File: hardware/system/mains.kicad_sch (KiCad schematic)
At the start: 10 parts, among them M1 Mains inlet, M2 RCD, M3 E-stop mushroom NC, M4 PSU 24-36 V, M5 Bit-change key switch, M6 Router contactor, M7 RC snubber, M8 Router socket, M9 PE: enclosure + lift frame

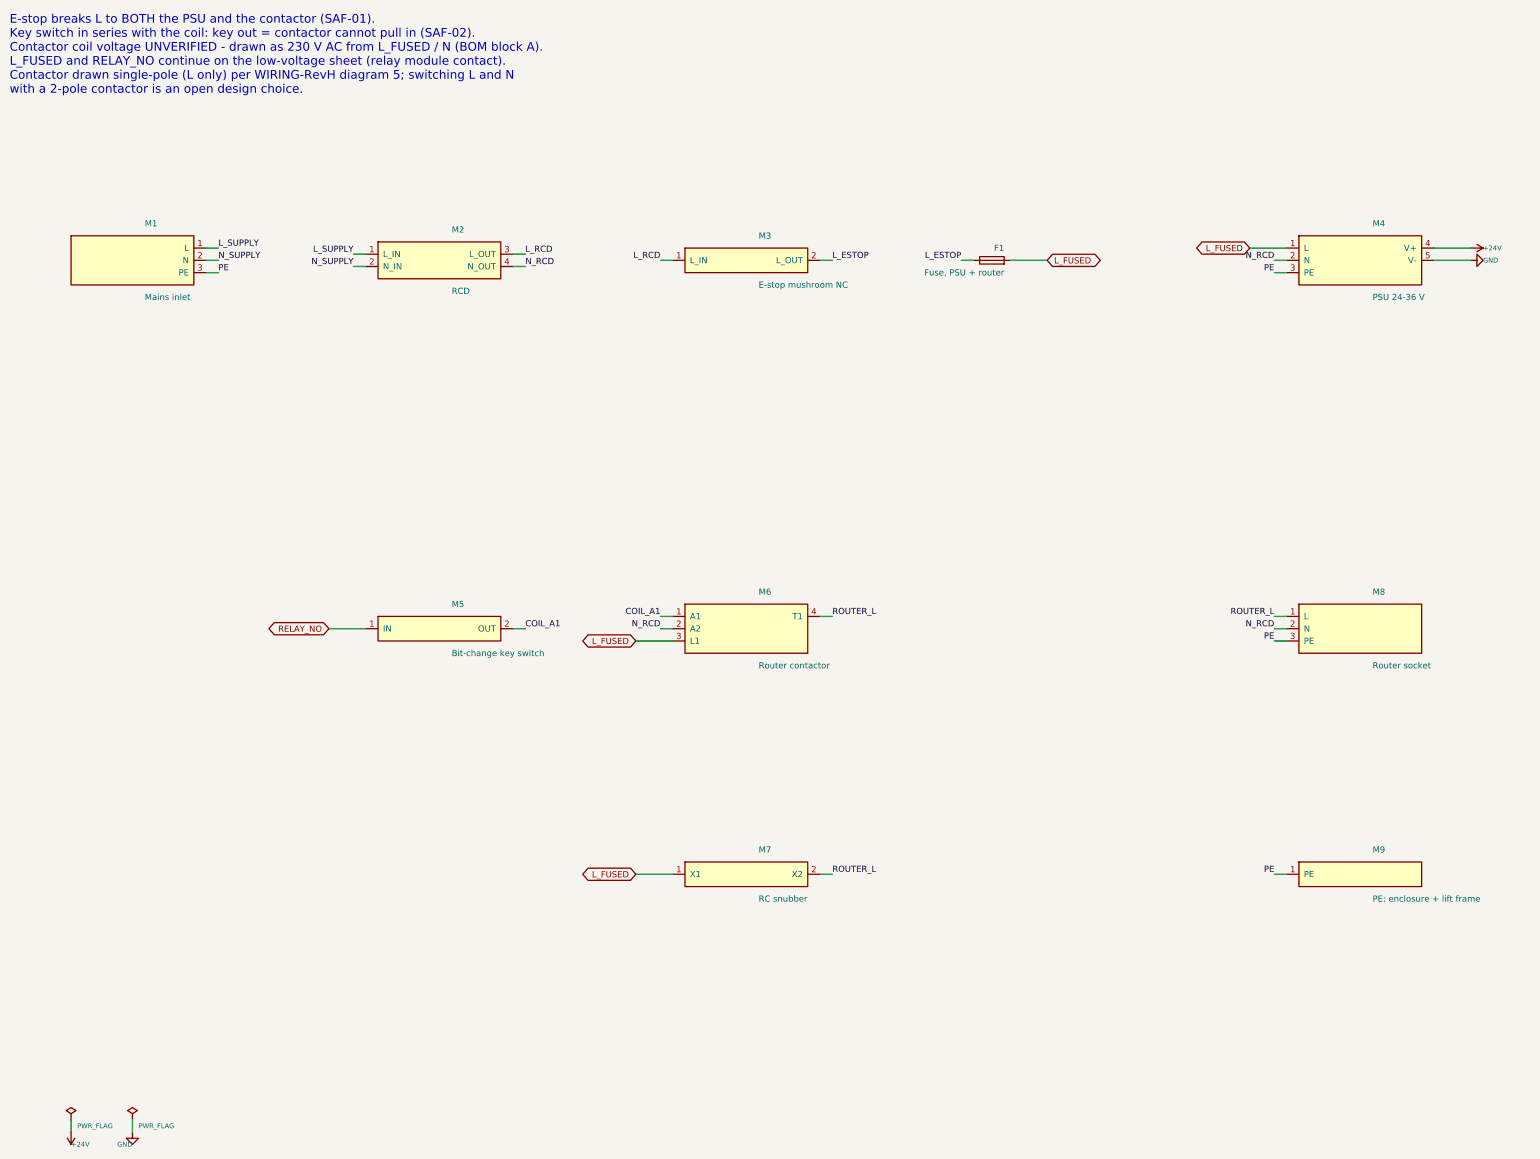
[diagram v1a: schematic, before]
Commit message: fix(hardware): put the fuse before the E-stop and switch L and N at the contactor
Decided 2026-09-14: the mains order is RCD, fuse, E-stop, and the
router contactor is 2-pole so the router is isolated whichever way
round the supply is wired. The live net after the E-stop is renamed
L_ESTOP. BOM block A, WIRING-RevH diagrams 1 and 5 and the spec now
agree with the drawing; the key switch stays between the relay
contact and coil A1.

Co-Authored-By: Claude Opus 5 (1M context) <noreply@anthropic.com>
Claude-Session: https://claude.ai/code/session_01N1nWXzYgvFT6pqfHGhLK6P
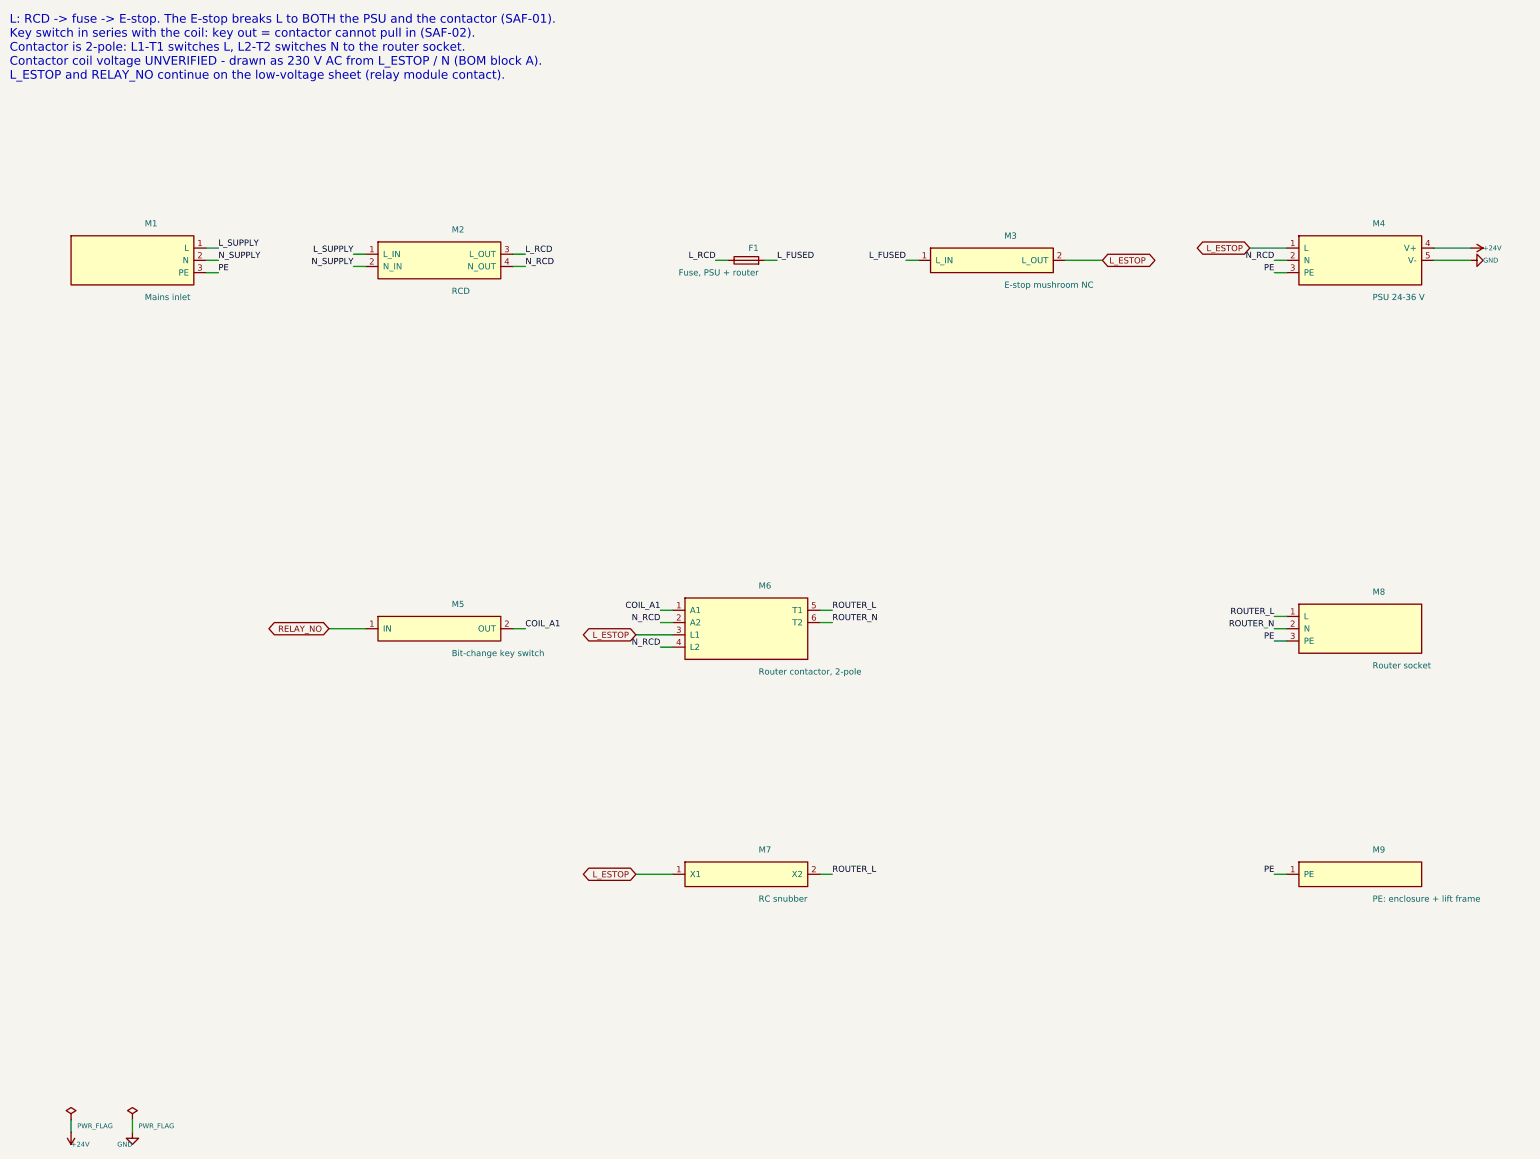
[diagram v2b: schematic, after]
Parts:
- F1: renamed from M3; value E-stop mushroom NC -> Fuse, PSU + router; symbol routerlift:ESTOP_NC -> Device:Fuse
- M3: renamed from F1; value Fuse, PSU + router -> E-stop mushroom NC; symbol Device:Fuse -> routerlift:ESTOP_NC
- M6: value Router contactor -> Router contactor, 2-pole
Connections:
- net L_ESTOP: now also M3.2 (L_OUT), M4.1 (L), M6.3 (L1), M7.1 (X1); no longer F1.2 (L_OUT), M3.1
- net L_FUSED: now also F1.2, M3.1 (L_IN); no longer M3.2, M4.1 (L), M6.3 (L1), M7.1 (X1)
- net N_RCD: now also M6.4 (L2); no longer M8.2 (N)
- net ROUTER_L: now also M6.5 (T1); no longer M6.4 (T1)
- new net ROUTER_N: M6.6 (T2), M8.2 (N)
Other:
- note added: "L: RCD -> fuse -> E-stop. The E-stop breaks L to BOTH the PSU and the contactor (SAF-01). Key switch in series with the coil: key out = contactor cannot pull in (SAF-02). Contactor is 2-pole: L1-T1 switches L, L2-T2 switches N to the router socket. Contactor coil voltage UNVERIFIED - drawn as 230 V AC from L_ESTOP / N (BOM block A). L_ESTOP and RELAY_NO continue on the low-voltage sheet (relay mo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"
- note removed: "E-stop breaks L to BOTH the PSU and the contactor (SAF-01). Key switch in series with the coil: key out = contactor cannot pull in (SAF-02). Contactor coil voltage UNVERIFIED - drawn as 230 V AC from L_FUSED / N (BOM block A). L_FUSED and RELAY_NO continue on the low-voltage sheet (relay module contact). Contactor drawn single-pole (L only) per WIRING-RevH diagram 5; switching L and N with a 2-po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"
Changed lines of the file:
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@@
 	(wire
 		(pts
-			(xy 162.56 76.2)
-			(xy 160.02 76.2))
+			(xy 173.99 76.2)
+			(xy 171.45 76.2))
 		(stroke
 			(width 0)
@@
 )
 	(label "L_RCD"
-		(at 160.02 76.2 180)
-		(effects
-			(font
-				(size 1.27 1.27))
-			(justify right bottom))
-)
-	(wire
-		(pts
-			(xy 193.04 76.2)
-			(xy 195.58 76.2))
-		(stroke
-			(width 0)
-			(type default))
-)
-	(label "L_ESTOP"
-		(at 195.58 76.2 0)
+		(at 171.45 76.2 180)
+		(effects
+			(font
+				(size 1.27 1.27))
+			(justify right bottom))
+)
+	(wire
+		(pts
+			(xy 181.61 76.2)
+			(xy 184.15 76.2))
+		(stroke
+			(width 0)
+			(type default))
+)
+	(label "L_FUSED"
+		(at 184.15 76.2 0)
 		(effects
 			(font
@@
 	(wire
 		(pts
-			(xy 224.79 76.2)
-			(xy 222.25 76.2))
-		(stroke
-			(width 0)
-			(type default))
-)
-	(label "L_ESTOP"
-		(at 222.25 76.2 180)
-		(effects
-			(font
-				(size 1.27 1.27))
-			(justify right bottom))
-)
-	(wire
-		(pts
-			(xy 232.41 76.2)
-			(xy 240.03 76.2))
-		(stroke
-			(width 0)
-			(type default))
-)
-	(global_label "L_FUSED"
+			(xy 213.36 76.2)
+			(xy 210.82 76.2))
+		(stroke
+			(width 0)
+			(type default))
+)
+	(label "L_FUSED"
+		(at 210.82 76.2 180)
+		(effects
+			(font
+				(size 1.27 1.27))
+			(justify right bottom))
+)
+	(wire
+		(pts
+			(xy 243.84 76.2)
+			(xy 251.46 76.2))
+		(stroke
+			(width 0)
+			(type default))
+)
+	(global_label "L_ESTOP"
 		(shape bidirectional)
-		(at 240.03 76.2 0)
+		(at 251.46 76.2 0)
 		(effects
 			(font
@@
 			(justify left))
 		(property "Intersheetrefs" "${INTERSHEET_REFS}"
-			(at 240.03 76.2 0)
+			(at 251.46 76.2 0)
 			(effects
 				(font
@@
 			(type default))
 )
-	(global_label "L_FUSED"
+	(global_label "L_ESTOP"
 		(shape bidirectional)
 		(at 281.94 73.66 180)
@@
 	(wire
 		(pts
-			(xy 162.56 149.86)
-			(xy 160.02 149.86))
+			(xy 162.56 148.59)
+			(xy 160.02 148.59))
 		(stroke
 			(width 0)
@@
 )
 	(label "COIL_A1"
-		(at 160.02 149.86 180)
-		(effects
-			(font
-				(size 1.27 1.27))
-			(justify right bottom))
-)
-	(wire
-		(pts
-			(xy 162.56 152.4)
-			(xy 160.02 152.4))
+		(at 160.02 148.59 180)
+		(effects
+			(font
+				(size 1.27 1.27))
+			(justify right bottom))
+)
+	(wire
+		(pts
+			(xy 162.56 151.13)
+			(xy 160.02 151.13))
 		(stroke
 			(width 0)
@@
 )
 	(label "N_RCD"
-		(at 160.02 152.4 180)
-		(effects
-			(font
-				(size 1.27 1.27))
-			(justify right bottom))
-)
-	(wire
-		(pts
-			(xy 162.56 154.94)
-			(xy 154.94 154.94))
-		(stroke
-			(width 0)
-			(type default))
-)
-	(global_label "L_FUSED"
+		(at 160.02 151.13 180)
+		(effects
+			(font
+				(size 1.27 1.27))
+			(justify right bottom))
+)
+	(wire
+		(pts
+			(xy 162.56 153.67)
+			(xy 154.94 153.67))
+		(stroke
+			(width 0)
+			(type default))
+)
+	(global_label "L_ESTOP"
 		(shape bidirectional)
-		(at 154.94 154.94 180)
+		(at 154.94 153.67 180)
 		(effects
 			(font
@@
 			(justify right))
 		(property "Intersheetrefs" "${INTERSHEET_REFS}"
-			(at 154.94 154.94 0)
+			(at 154.94 153.67 0)
 			(effects
 				(font
@@
 	(wire
 		(pts
-			(xy 193.04 149.86)
-			(xy 195.58 149.86))
+			(xy 162.56 156.21)
+			(xy 160.02 156.21))
+		(stroke
+			(width 0)
+			(type default))
+)
+	(label "N_RCD"
+		(at 160.02 156.21 180)
+		(effects
+			(font
+				(size 1.27 1.27))
+			(justify right bottom))
+)
+	(wire
+		(pts
+			(xy 193.04 148.59)
+			(xy 195.58 148.59))
 		(stroke
 			(width 0)
@@
 )
 	(label "ROUTER_L"
-		(at 195.58 149.86 0)
+		(at 195.58 148.59 0)
+		(effects
+			(font
+				(size 1.27 1.27))
+			(justify left bottom))
+)
+	(wire
+		(pts
+			(xy 193.04 151.13)
+			(xy 195.58 151.13))
+		(stroke
+			(width 0)
+			(type default))
+)
+	(label "ROUTER_N"
+		(at 195.58 151.13 0)
 		(effects
 			(font
@@
 			(type default))
 )
-	(global_label "L_FUSED"
+	(global_label "L_ESTOP"
 		(shape bidirectional)
 		(at 154.94 203.2 180)
@@
 			(type default))
 )
-	(label "N_RCD"
+	(label "ROUTER_N"
 		(at 287.02 152.4 180)
 		(effects
@@
 			(type default))
 )
-	(text "E-stop breaks L to BOTH the PSU and the contactor (SAF-01).\nKey switch in series with the coil: key out = contactor cannot pull in (SAF-02).\nContactor coil voltage UNVERIFIED - drawn as 230 V AC from L_FUSED / N (BOM block A).\nL_FUSED and RELAY_NO continue on the low-voltage sheet (relay module contact).\nContactor drawn single-pole (L only) per WIRING-RevH diagram 5; switching L and N\nwith a 2-pole contactor is an open design choice."
+	(text "L: RCD -> fuse -> E-stop. The E-stop breaks L to BOTH the PSU and the contactor (SAF-01).\nKey switch in series with the coil: key out = contactor cannot pull in (SAF-02).\nContactor is 2-pole: L1-T1 switches L, L2-T2 switches N to the router socket.\nContactor coil voltage UNVERIFIED - drawn as 230 V AC from L_ESTOP / N (BOM block A).\nL_ESTOP and RELAY_NO continue on the low-voltage sheet (relay module contact)."
 		(exclude_from_sim no)
 		(at 25.4 25.4 0)
@@
 					(unit 1)))))
 	(symbol
-		(lib_id "routerlift:ESTOP_NC")
-		(at 177.8 76.2 0)
+		(lib_id "Device:Fuse")
+		(at 177.8 76.2 90)
 		(unit 1)
 		(exclude_from_sim no)
@@
 		(on_board yes)
 		(dnp no)
+		(property "Reference" "F1"
+			(at 180.34 73.66 90)
+			(effects
+				(font
+					(size 1.27 1.27))
+				(justify left)))
+		(property "Value" "Fuse, PSU + router"
+			(at 180.34 78.74 90)
+			(effects
+				(font
+					(size 1.27 1.27))
+				(justify left)))
+		(property "Footprint" ""
+			(at 177.8 76.2 90)
+			(effects
+				(font
+					(size 1.27 1.27))
+				(justify left)
+				(hide yes)))
+		(property "Datasheet" ""
+			(at 177.8 76.2 90)
+			(effects
+				(font
+					(size 1.27 1.27))
+				(justify left)
+				(hide yes)))
+		(pin "1"
+)
+		(pin "2"
+)
+		(instances
+			(project "system"
+				(path "/582f3ed4-e62a-52c1-8184-c0dfd7f587a1/fcef0137-bbe8-5222-9af7-39540385d8c5"
+					(reference "F1")
+					(unit 1)))))
+	(symbol
+		(lib_id "routerlift:ESTOP_NC")
+		(at 228.6 76.2 0)
+		(unit 1)
+		(exclude_from_sim no)
+		(in_bom yes)
+		(on_board yes)
+		(dnp no)
 		(property "Reference" "M3"
-			(at 180.34 71.12 0)
+			(at 231.14 71.12 0)
 			(effects
 				(font
@@
 				(justify left)))
 		(property "Value" "E-stop mushroom NC"
-			(at 180.34 81.28 0)
-			(effects
-				(font
-					(size 1.27 1.27))
-				(justify left)))
-		(property "Footprint" ""
-			(at 177.8 76.2 0)
-			(effects
-				(font
-					(size 1.27 1.27))
-				(justify left)
-				(hide yes)))
-		(property "Datasheet" ""
-			(at 177.8 76.2 0)
+			(at 231.14 81.28 0)
+			(effects
+				(font
+					(size 1.27 1.27))
+				(justify left)))
+		(property "Footprint" ""
+			(at 228.6 76.2 0)
+			(effects
+				(font
+					(size 1.27 1.27))
+				(justify left)
+				(hide yes)))
+		(property "Datasheet" ""
+			(at 228.6 76.2 0)
 			(effects
 				(font
@@
 					(unit 1)))))
 	(symbol
-		(lib_id "Device:Fuse")
-		(at 228.6 76.2 90)
-		(unit 1)
-		(exclude_from_sim no)
-		(in_bom yes)
-		(on_board yes)
-		(dnp no)
-		(property "Reference" "F1"
-			(at 231.14 73.66 90)
-			(effects
-				(font
-					(size 1.27 1.27))
-				(justify left)))
-		(property "Value" "Fuse, PSU + router"
-			(at 231.14 78.74 90)
-			(effects
-				(font
-					(size 1.27 1.27))
-				(justify left)))
-		(property "Footprint" ""
-			(at 228.6 76.2 90)
-			(effects
-				(font
-					(size 1.27 1.27))
-				(justify left)
-				(hide yes)))
-		(property "Datasheet" ""
-			(at 228.6 76.2 90)
-			(effects
-				(font
-					(size 1.27 1.27))
-				(justify left)
-				(hide yes)))
-		(pin "1"
-)
-		(pin "2"
-)
-		(instances
-			(project "system"
-				(path "/582f3ed4-e62a-52c1-8184-c0dfd7f587a1/fcef0137-bbe8-5222-9af7-39540385d8c5"
-					(reference "F1")
-					(unit 1)))))
-	(symbol
 		(lib_id "routerlift:PSU_24_36V")
 		(at 304.8 76.2 0)
@@
 		(dnp no)
 		(property "Reference" "M6"
-			(at 180.34 144.78 0)
-			(effects
-				(font
-					(size 1.27 1.27))
-				(justify left)))
-		(property "Value" "Router contactor"
-			(at 180.34 160.02 0)
+			(at 180.34 143.51 0)
+			(effects
+				(font
+					(size 1.27 1.27))
+				(justify left)))
+		(property "Value" "Router contactor, 2-pole"
+			(at 180.34 161.29 0)
 			(effects
 				(font
@@
 		(pin "4"
 )
-		(instances
+		(pin "5"
+)
+		(pin "6"
+)
+		(instances
